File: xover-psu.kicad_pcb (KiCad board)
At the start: 2 copper layers, 100 x 100 mm, 107 parts, among them J1 Screw_Terminal_01x03, J2 Screw_Terminal_01x02, J3 Screw_Terminal_01x02, J4 Screw_Terminal_01x03, J5 Screw_Terminal_01x03, J6 Screw_Terminal_01x02, J7 Screw_Terminal_01x02, J8 Screw_Terminal_01x03, K2 T9GS1L14-12, Q1 AO3400, Q2 2N7002, Q3 AO3400, U1 817C, U2 TL431DBZ, U4 LM317_3PinPackage, U5 LM337_TO220, U6 TL431DBZ, U8 817C

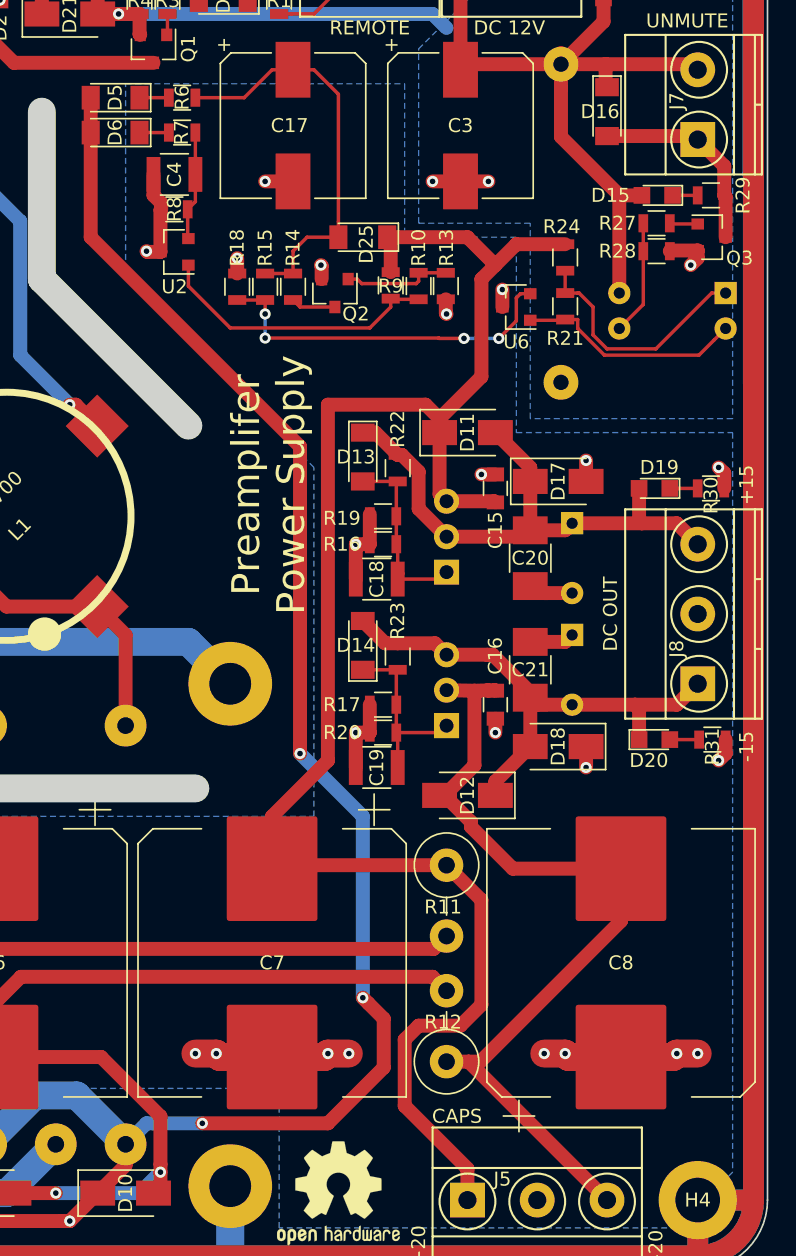
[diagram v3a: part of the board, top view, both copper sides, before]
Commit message: better AGND plane divide, regenerated layout png
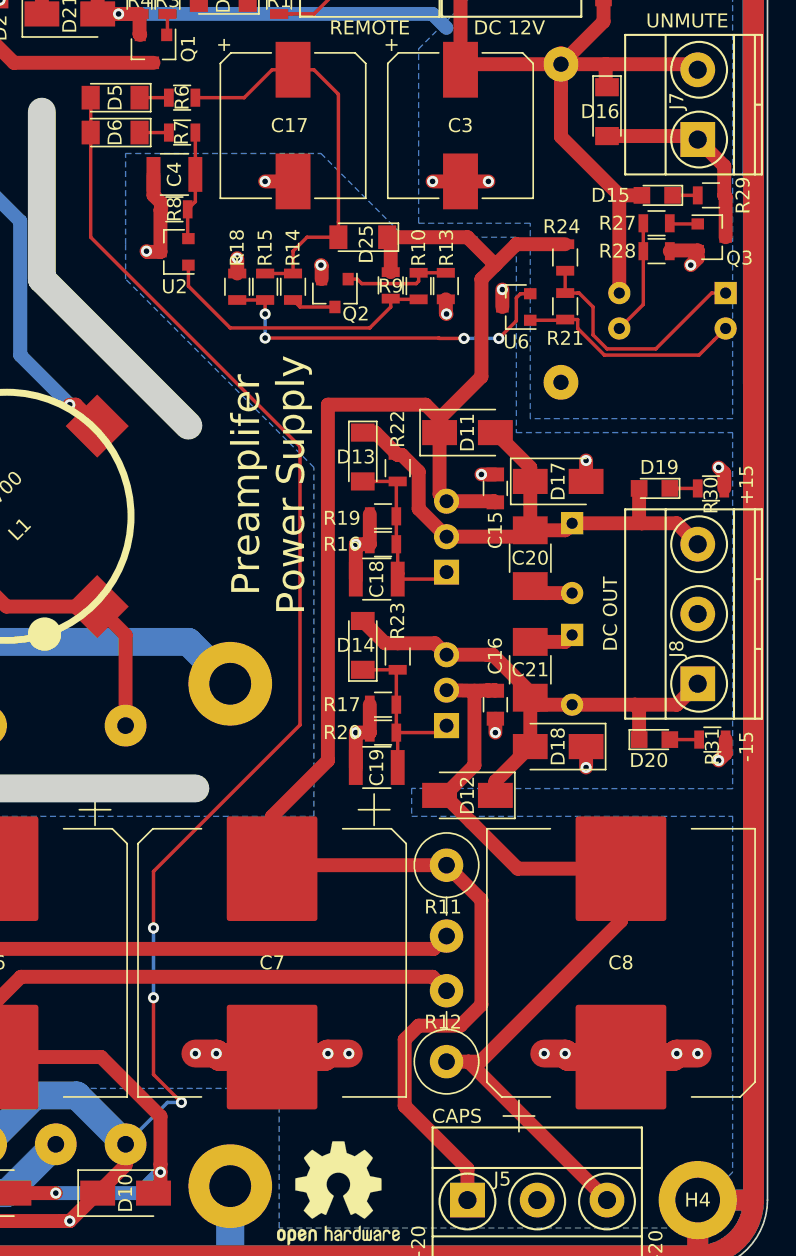
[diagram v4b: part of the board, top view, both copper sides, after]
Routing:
- net /AC2: track 135.2 -> 124.8 mm
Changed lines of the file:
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@@
     (thickness 1)
     (drawings 75)
-    (tracks 593)
+    (tracks 588)
     (zones 0)
     (modules 107)
@@
   (layers
     (0 F.Cu signal)
-    (31 B.Cu signal hide)
-    (32 B.Adhes user)
+    (31 B.Cu signal)
+    (32 B.Adhes user hide)
     (33 F.Adhes user hide)
     (34 B.Paste user hide)
     (35 F.Paste user hide)
-    (36 B.SilkS user)
-    (37 F.SilkS user)
-    (38 B.Mask user)
-    (39 F.Mask user)
+    (36 B.SilkS user hide)
+    (37 F.SilkS user hide)
+    (38 B.Mask user hide)
+    (39 F.Mask user hide)
     (40 Dwgs.User user hide)
     (41 Cmts.User user hide)
@@
     (44 Edge.Cuts user)
     (45 Margin user)
-    (46 B.CrtYd user hide)
+    (46 B.CrtYd user)
     (47 F.CrtYd user)
     (48 B.Fab user hide)
@@
     (aux_axis_origin 0 0)
     (grid_origin 25 25)
-    (visible_elements FFFFFF7F)
+    (visible_elements FFFFEF7F)
     (pcbplotparams
       (layerselection 0x110f0_ffffffff)
@@
   (via (at 64 119.5) (size 0.8) (drill 0.4) (layers F.Cu B.Cu) (net 17))
   (segment (start 80 43.5) (end 82.1 43.5) (width 0.25) (layer F.Cu) (net 18))
-  (segment (start 76.5 43.5) (end 76.5 41) (width 1) (layer F.Cu) (net 19))
-  (via (at 91.5 87.999996) (size 0.8) (drill 0.4) (layers F.Cu B.Cu) (net 19))
-  (segment (start 91.5 87.434311) (end 91.5 87.999996) (width 1) (layer F.Cu) (net 19))
-  (segment (start 76.5 43.5) (end 76.5 51) (width 1) (layer F.Cu) (net 19))
-  (segment (start 76.5 51) (end 91.5 66) (width 1) (layer F.Cu) (net 19))
-  (segment (start 91.5 66) (end 91.5 87.434311) (width 1) (layer F.Cu) (net 19))
+  (segment (start 76.5 43.5) (end 76.5 41) (width 0.25) (layer F.Cu) (net 19))
   (segment (start 61 120.5) (end 61.5 120) (width 1) (layer F.Cu) (net 19))
   (segment (start 61 120.5) (end 61 119.5) (width 1) (layer F.Cu) (net 19))
-  (via (at 84.5 114.5) (size 0.8) (drill 0.4) (layers F.Cu B.Cu) (net 19))
-  (segment (start 80.501109 114.501371) (end 80.998629 114.501371) (width 1) (layer B.Cu) (net 19))
-  (segment (start 79.00124 116.00124) (end 80.501109 114.501371) (width 1) (layer B.Cu) (net 19))
-  (segment (start 81 114.5) (end 84.5 114.5) (width 1) (layer B.Cu) (net 19))
-  (segment (start 80.998629 114.501371) (end 81 114.5) (width 1) (layer B.Cu) (net 19))
   (segment (start 75.5 112.5) (end 79.00124 116.00124) (width 2) (layer B.Cu) (net 19))
   (segment (start 72.5025 112.5) (end 75.5 112.5) (width 2) (layer B.Cu) (net 19))
   (segment (start 69.00126 116.00124) (end 72.5025 112.5) (width 2) (layer B.Cu) (net 19))
-  (segment (start 96.399999 105.899999) (end 96 105.5) (width 1) (layer F.Cu) (net 19))
-  (segment (start 97.5 107) (end 96.399999 105.899999) (width 1) (layer F.Cu) (net 19))
-  (segment (start 97.5 110.5) (end 97.5 107) (width 1) (layer F.Cu) (net 19))
-  (segment (start 93.5 114.5) (end 97.5 110.5) (width 1) (layer F.Cu) (net 19))
-  (segment (start 84.5 114.5) (end 93.5 114.5) (width 1) (layer F.Cu) (net 19))
-  (segment (start 96 92.499996) (end 96 105.5) (width 1) (layer B.Cu) (net 19))
-  (segment (start 91.5 87.999996) (end 96 92.499996) (width 1) (layer B.Cu) (net 19))
-  (via (at 96 105.5) (size 0.8) (drill 0.4) (layers F.Cu B.Cu) (net 19))
   (via (at 74.999998 121.5) (size 0.8) (drill 0.4) (layers F.Cu B.Cu) (net 19))
   (segment (start 62 121.5) (end 74.434313 121.5) (width 1) (layer F.Cu) (net 19))
@@
   (segment (start 79.00124 117.49876) (end 75 121.5) (width 1) (layer F.Cu) (net 19))
   (segment (start 79.00124 116.00124) (end 79.00124 117.49876) (width 1) (layer F.Cu) (net 19))
+  (via (at 81 100.5) (size 0.8) (drill 0.4) (layers F.Cu B.Cu) (net 19))
+  (segment (start 81 100.5) (end 81 105.5) (width 0.25) (layer B.Cu) (net 19))
+  (via (at 81 105.5) (size 0.8) (drill 0.4) (layers F.Cu B.Cu) (net 19))
+  (segment (start 76.5 51) (end 76.5 43.5) (width 0.25) (layer F.Cu) (net 19))
+  (segment (start 91.5 66) (end 76.5 51) (width 0.25) (layer F.Cu) (net 19))
+  (segment (start 91.5 85.952089) (end 91.5 66) (width 0.25) (layer F.Cu) (net 19))
+  (segment (start 81 96.452089) (end 91.5 85.952089) (width 0.25) (layer F.Cu) (net 19))
+  (segment (start 81 100.5) (end 81 96.452089) (width 0.25) (layer F.Cu) (net 19))
+  (via (at 82.999998 113) (size 0.8) (drill 0.4) (layers F.Cu B.Cu) (net 19))
+  (segment (start 79.00124 116.00124) (end 82.00248 113) (width 0.25) (layer B.Cu) (net 19))
+  (segment (start 82.00248 113) (end 82.999998 113) (width 0.25) (layer B.Cu) (net 19))
+  (segment (start 81 105.5) (end 81 111.000002) (width 0.25) (layer F.Cu) (net 19))
+  (segment (start 81 111.000002) (end 82.599999 112.600001) (width 0.25) (layer F.Cu) (net 19))
+  (segment (start 82.599999 112.600001) (end 82.999998 113) (width 0.25) (layer F.Cu) (net 19))
   (segment (start 120 48) (end 118.2 48) (width 0.25) (layer F.Cu) (net 20))
   (segment (start 119.75 43.75) (end 120 44) (width 1) (layer F.Cu) (net 21))
@@
   (segment (start 114.5 100) (end 114.5 96.25) (width 1) (layer F.Cu) (net 47))
   (segment (start 104.42 110.08) (end 114.5 100) (width 1) (layer F.Cu) (net 47))
-  (segment (start 103.75 92.9) (end 101.85 91) (width 1) (layer F.Cu) (net 47))
-  (segment (start 103.75 93.25) (end 103.75 92.9) (width 1) (layer F.Cu) (net 47))
-  (segment (start 106.75 96.25) (end 103.75 93.25) (width 1) (layer F.Cu) (net 47))
-  (segment (start 114.5 96.25) (end 106.75 96.25) (width 1) (layer F.Cu) (net 47))
   (segment (start 104.96 83.46) (end 105 83.5) (width 1) (layer F.Cu) (net 47))
   (segment (start 105.46 83.46) (end 105.5 83.5) (width 1) (layer F.Cu) (net 47))
@@
   (segment (start 104 83.5) (end 105.46 83.46) (width 1) (layer F.Cu) (net 47))
   (segment (start 102 83.46) (end 104 83.5) (width 1) (layer F.Cu) (net 47))
+  (segment (start 103.75 92.9) (end 101.85 91) (width 1) (layer F.Cu) (net 47))
+  (segment (start 107.1 96.25) (end 103.75 92.9) (width 1) (layer F.Cu) (net 47))
+  (segment (start 114.5 96.25) (end 107.1 96.25) (width 1) (layer F.Cu) (net 47))
   (segment (start 38 99) (end 38 102.75) (width 1.5) (layer F.Cu) (net 48))
   (segment (start 38 116) (end 38 114.5) (width 1) (layer F.Cu) (net 49))
@@
     (polygon
       (pts
-        (xy 122.5 118) (xy 118.5 122) (xy 90 122) (xy 90 112) (xy 44 112)
-        (xy 44 92.5) (xy 92.5 92.5) (xy 92.5 67.5) (xy 79 54) (xy 79 40)
-        (xy 99 40) (xy 99 51) (xy 107 51) (xy 107 65) (xy 122.5 65)
+        (xy 122.5 90.522276) (xy 99.5 90.5) (xy 99.5 92.5) (xy 122.5 92.5) (xy 122.5 118)
+        (xy 118.5 122) (xy 90 122) (xy 90 112) (xy 44 112) (xy 44 92.5)
+        (xy 92.5 92.5) (xy 92.5 67.5) (xy 79 54) (xy 79 51.5) (xy 79 45)
+        (xy 93 45) (xy 99 51) (xy 107 51) (xy 107 65) (xy 122.5 65)
       )
     )

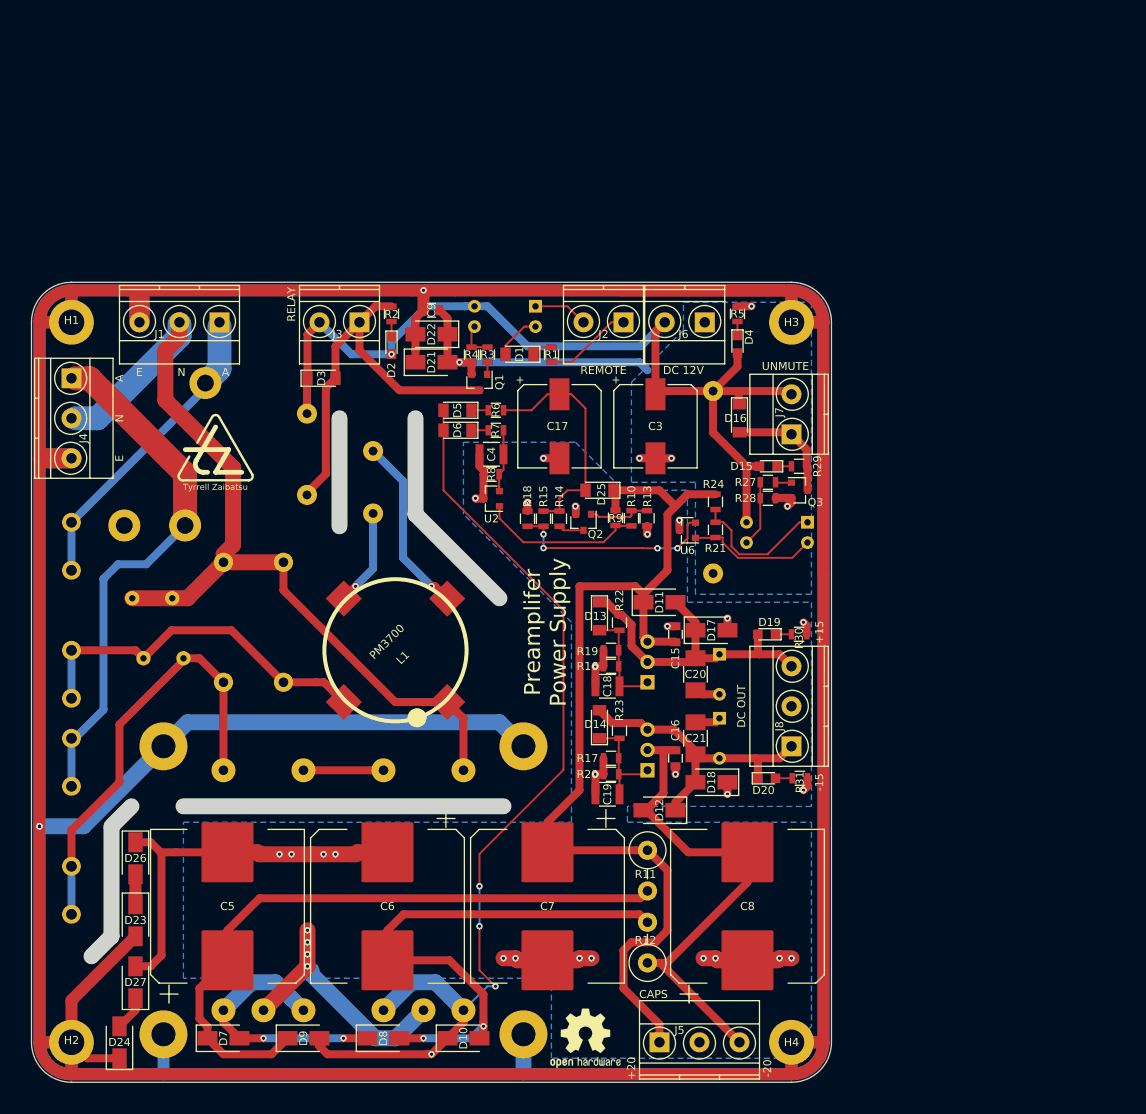
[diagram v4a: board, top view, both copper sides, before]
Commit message: updated schematic for faster turn-on transition for UNMUTE
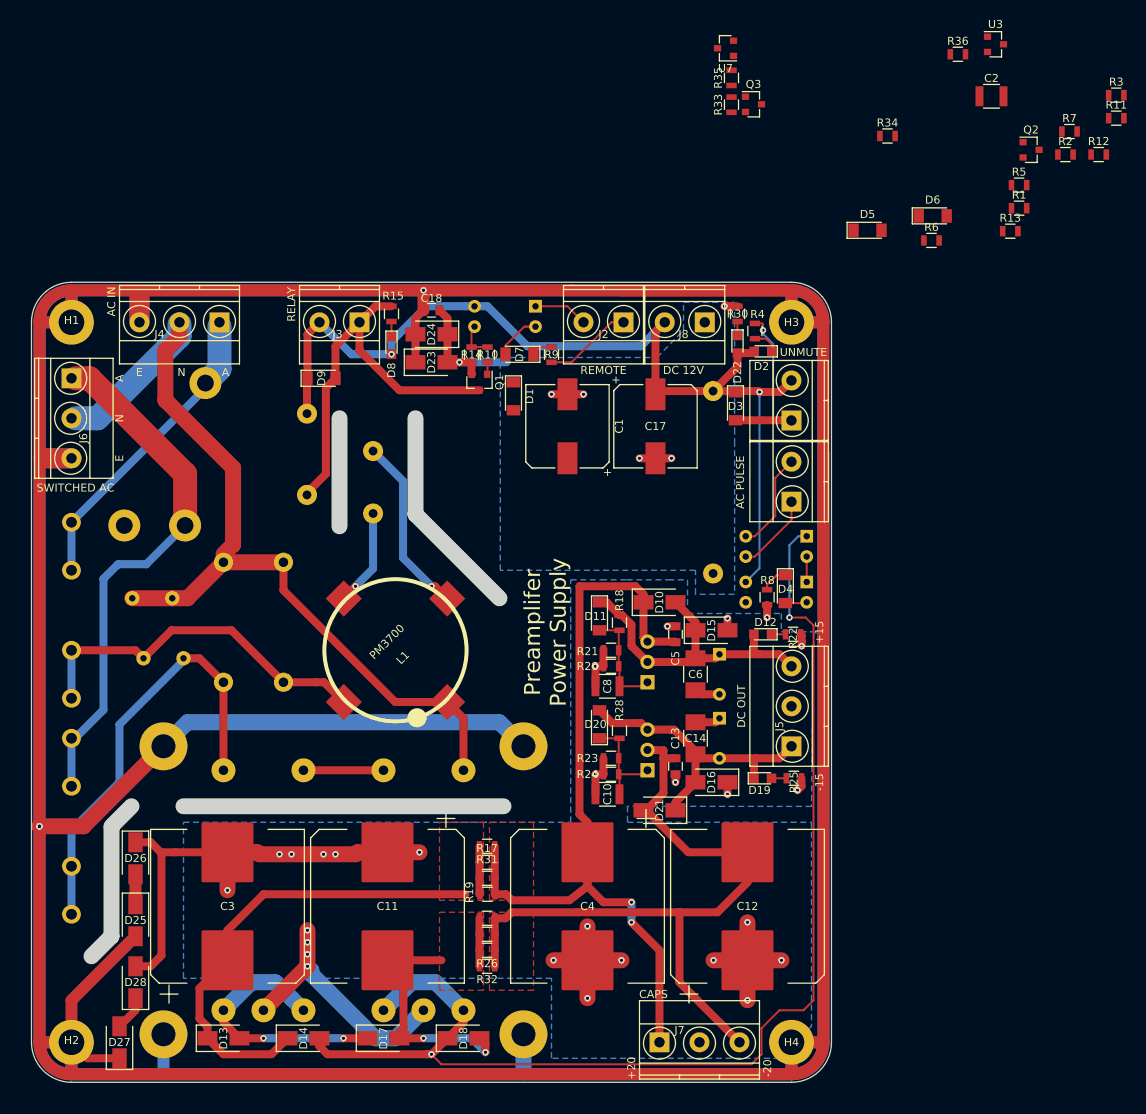
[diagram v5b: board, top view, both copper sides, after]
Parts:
- removed the C17 at (91.0, 43.0)
- removed the C4 at (82.5, 46.5)
- removed the D15 at (117.1, 48.0)
- removed the D16 at (113.5, 42.0)
- removed the D25 at (96.0, 51.0)
- removed the J7 at (120.0, 44.0)
- removed the R10 at (100.0, 54.5)
- removed the R14 at (91.0, 54.5)
- removed the R15 at (89.0, 54.5)
- removed the R18 at (87.0, 54.5)
- removed the R21 at (110.5, 56.0)
- removed the R24 at (110.5, 52.5)
- removed the R28 at (117.0, 52.0)
- removed the R9 at (98.0, 54.5)
- removed REF**: Tyrrell Zaibatsu, tz:Tyrrell-Zaibatsu-20-Back
- removed REF**: Tyrrell Zaibatsu, tz:Tyrrell-Zaibatsu-10
- removed REF***: OSHW-Symbol_6.7x6mm_SilkScreen, pcb:OSHW-Symbol_6.7x6mm_BackSilkScreen
- removed REF***: OSHW-Logo2_9.8x8mm_SilkScreen, Symbols:OSHW-Logo2_9.8x8mm_SilkScreen
- removed the U2 at (82.5, 52.0)
- removed U8: 817C, Housings_DIP:DIP-4_W7.62mm_Socket
- added C1: 220u, Capacitors_SMD:CP_Elec_10x10, F.Cu at (92.0, 43.0)
- added C2: 10u, Capacitors_SMD:C_1210, F.Cu at (145.0, 1.75)
- added D1: LL4148, Diodes_SMD:D_MiniMELF, F.Cu at (85.2, 39.2)
- added D2: LED, LEDs:LED_0805, F.Cu at (116.4, 33.6)
- added D3: LL4148, Diodes_SMD:D_MiniMELF, F.Cu at (113.0, 40.5)
- added D4: LL4148, Diodes_SMD:D_MiniMELF, F.Cu at (119.2, 63.4)
- added J1: Screw_Terminal_01x02, Terminals_Phoenix:TerminalBlock_Phoenix_MKDS1.5-2pol, F.Cu at (120.0, 42.3)
- added J9: Screw_Terminal_01x02, Terminals_Phoenix:TerminalBlock_Phoenix_MKDS1.5-2pol, F.Cu at (120.0, 52.4)
- added R1: 3k9, Resistors_SMD:R_0805, F.Cu at (148.4, 15.7)
- added R11: 4k7, Resistors_SMD:R_0805, F.Cu at (160.6, 4.49)
- added R16: 4R7, Resistors_SMD:R_0805, F.Cu at (82.0, 99.5)
- added R17: 4R7, Resistors_SMD:R_0805, F.Cu at (82.0, 97.5)
- added R2: 2k, Resistors_SMD:R_0805, F.Cu at (154.2, 9.04)
- added R26: 4R7, Resistors_SMD:R_0805, F.Cu at (82.0, 108.5)
- added R3: 20k, Resistors_SMD:R_0805, F.Cu at (160.6, 1.60)
- added R31: 4R7, Resistors_SMD:R_0805, F.Cu at (82.0, 95.5)
- added R32: 4R7, Resistors_SMD:R_0805, F.Cu at (82.0, 110.5)
- added R33: 430, Resistors_SMD:R_0805, F.Cu at (112.5, 2.80)
- added R34: 10k, Resistors_SMD:R_0805, F.Cu at (132.0, 6.71)
- added R35: 680, Resistors_SMD:R_0805, F.Cu at (112.5, -0.55)
- added R36: 10k, Resistors_SMD:R_0805, F.Cu at (140.8, -3.50)
- added R4: 3k9, Resistors_SMD:R_0805, F.Cu at (115.4, 31.1)
- added R5: 2k, Resistors_SMD:R_0805, F.Cu at (148.4, 12.9)
- added U1: 817C, Housings_DIP:DIP-4_W7.62mm_Socket, B.Cu at (121.9, 62.5)
- added U3: TL431DBZ, TO_SOT_Packages_SMD:SOT-23, F.Cu at (145.5, -4.75)
- added U7: TL431DBZ, TO_SOT_Packages_SMD:SOT-23, F.Cu at (111.8, -4.25)
- Q3: value AO3400 -> AO3401A
- R12: value 5.6 -> 10k; footprint Resistors_ThroughHole:R_Axial_DIN0414_L11.9mm_D4.5mm_P5.08mm_Vertical -> Resistors_SMD:R_0805
- R19: renamed from R11; value 5.6 -> 4R7; footprint Resistors_ThroughHole:R_Axial_DIN0414_L11.9mm_D4.5mm_P5.08mm_Vertical -> Resistors_SMD:R_0805
- R27: value 100 -> 4R7
- R29: value 3k9 -> 4R7
- R6: value 4k7 -> 15k
- R7: value 4k7 -> 100
- R8: value 4k7 -> 3k9
- U6: value TL431DBZ -> 817C; footprint TO_SOT_Packages_SMD:SOT-23 -> Housings_DIP:DIP-4_W7.62mm_Socket; moved to B.Cu
- moved R12 115.7 mm to (158.4, 9.04), turned to 0 degrees
- moved R7 80.8 mm to (154.8, 6.16)
- moved Q2 72.8 mm to (149.9, 8.44), turned to 0 degrees
- moved R29 68.7 mm to (82.0, 104.5), turned to 180 degrees
- moved R27 66.5 mm to (82.0, 106.5)
- moved D6 65.2 mm to (137.7, 16.7), turned to 0 degrees
- moved R6 58.4 mm to (137.5, 19.8)
- moved R13 57.9 mm to (147.3, 18.6), turned to 0 degrees
- moved D5 56.0 mm to (129.5, 18.5), turned to 0 degrees
- moved Q3 48.6 mm to (115.2, 2.75)
- moved R8 37.7 mm to (116.9, 64.4), turned to 90 degrees
- moved R19 20.7 mm to (82.0, 101.5), turned to 180 degrees
- moved U6 14.9 mm to (121.9, 56.8)
- moved C4 5.00 mm to (94.5, 103.0)
- moved C13 1.00 mm to (105.5, 85.5)
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- renumbered C19 to C10, C6 to C11, C8 to C12, C16 to C13, C21 to C14, C23 to C15, C1 to C16, C3 to C17, C9 to C18, C5 to C3, C7 to C4, C15 to C5, C20 to C6, C22 to C7, C18 to C8, C2 to C9, D11 to D10, D13 to D11, D19 to D12, D7 to D13, D9 to D14, D17 to D15, D18 to D16, D8 to D17, D10 to D18, D20 to D19, D14 to D20, D12 to D21, D4 to D22, D21 to D23, D22 to D24, D23 to D25, D24 to D27, D27 to D28, D1 to D7, D2 to D8, D3 to D9, F2 to F1, F1 to F2, J1 to J4, J8 to J5, J4 to J6, J5 to J7, J6 to J8, K2 to K1, R3 to R10, R4 to R14, R2 to R15, R22 to R18, R16 to R20, R19 to R21, R30 to R22, R17 to R23, R20 to R24, R31 to R25, R23 to R28, R5 to R30, R1 to R9, RV2 to RV1, RV1 to RV2, U1 to U2
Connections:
- D5 pad 2: /AC2 -> Net-(D5-Pad2)
- D6 pad 2: /AC2 -> Net-(D5-Pad2)
- Q2 pad 2: /AGND -> /DGND
- Q3 pad 2: /DGND -> /VDD
- Q3 pad 3: Net-(D16-Pad2) -> Net-(D2-Pad2)
- R12 pad 1: /RECT2B -> /DGND
- R12 pad 2: /RECT2 -> Net-(Q2-Pad1)
- R13 pad 1: /AGND -> Net-(R13-Pad1)
- R13 pad 2: Net-(Q2-Pad1) -> /DGND
- R27 pad 1: Net-(Q3-Pad1) -> /RECT2B
- R27 pad 2: Net-(R27-Pad2) -> /RECT2
- R29 pad 1: Net-(D15-Pad1) -> /RECT2B
- R29 pad 2: Net-(D16-Pad2) -> /RECT2
- R6 pad 1: Net-(D5-Pad1) -> Net-(R1-Pad1)
- R6 pad 2: Net-(C17-Pad1) -> Net-(Q2-Pad1)
- R7 pad 1: Net-(D6-Pad1) -> Net-(Q2-Pad3)
- R7 pad 2: Net-(C4-Pad1) -> Net-(C1-Pad1)
- R8 pad 1: Net-(C4-Pad1) -> /AGND
- R8 pad 2: /AGND -> Net-(D4-Pad1)
- U6 pad 1: Net-(R21-Pad2) -> /AC2
- U6 pad 3: /AGND -> Net-(J9-Pad1)
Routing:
- net /RECT2: track 67.9 -> 37.1 mm
- net Net-(C17-Pad1): track 29.3 -> 0.00 mm
- net /RECT2B: track 62.9 -> 91.0 mm
- net /AC2: track 124.8 -> 151.6 mm, vias 4 -> 2
- net /RECT1B: track 126.0 -> 100.1 mm, vias 0 -> 2
- net Net-(U1-Pad1): track 26.0 -> 3.18 mm, vias 4 -> 0
- net Net-(R10-Pad1): track 20.5 -> 0.00 mm
- net Net-(R21-Pad1): track 17.6 -> 0.00 mm
- net /RECT1: track 81.6 -> 64.7 mm
- net Net-(R21-Pad2): track 16.2 -> 0.00 mm
- net Net-(D16-Pad2): track 14.4 -> 0.00 mm
- net Net-(J9-Pad2): track 0.00 -> 12.4 mm
- net /AGND: track 143.1 -> 153.4 mm, vias 30 -> 27
- net Net-(J9-Pad1): track 0.00 -> 9.89 mm
- net Net-(R27-Pad2): track 8.25 -> 0.00 mm
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- added copper zone on F.Cu, net /RECT1
- added copper zone on F.Cu, net /RECT1B
- added copper zone on F.Cu, net /RECT2
- added copper zone on F.Cu, net /RECT2B
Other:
- board text added: "AC IN"
- board text added: "AC PULSE"
- board text added: "C"
- board text added: "Preamplifier Power Supply Rev.A 202110 william@brodie-tyrrell.org github.com/phenidone"
- board text removed: "AC LINE"
- board text removed: "Preamplifier Power Supply Rev.A 202110 github.com/phenidone"
